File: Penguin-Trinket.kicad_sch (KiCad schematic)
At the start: 17 parts, among them M1 Motor_DC, Q1 NPN, Q2 NPN, Q3 NPN, SW1 SW_Push

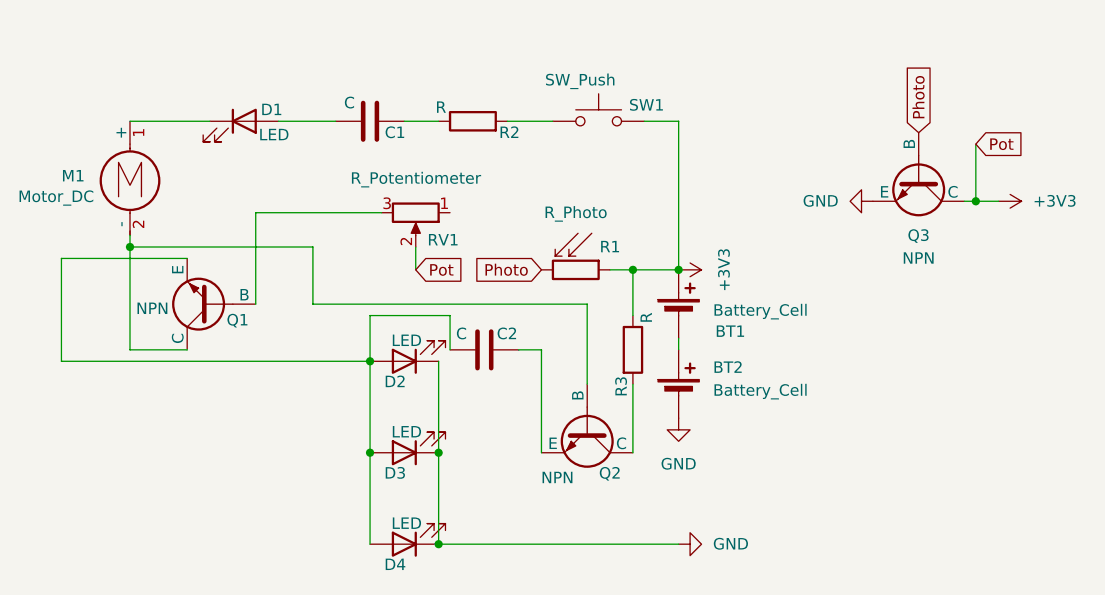
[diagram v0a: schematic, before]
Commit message: redo (trinket v3)
hopefully everything works
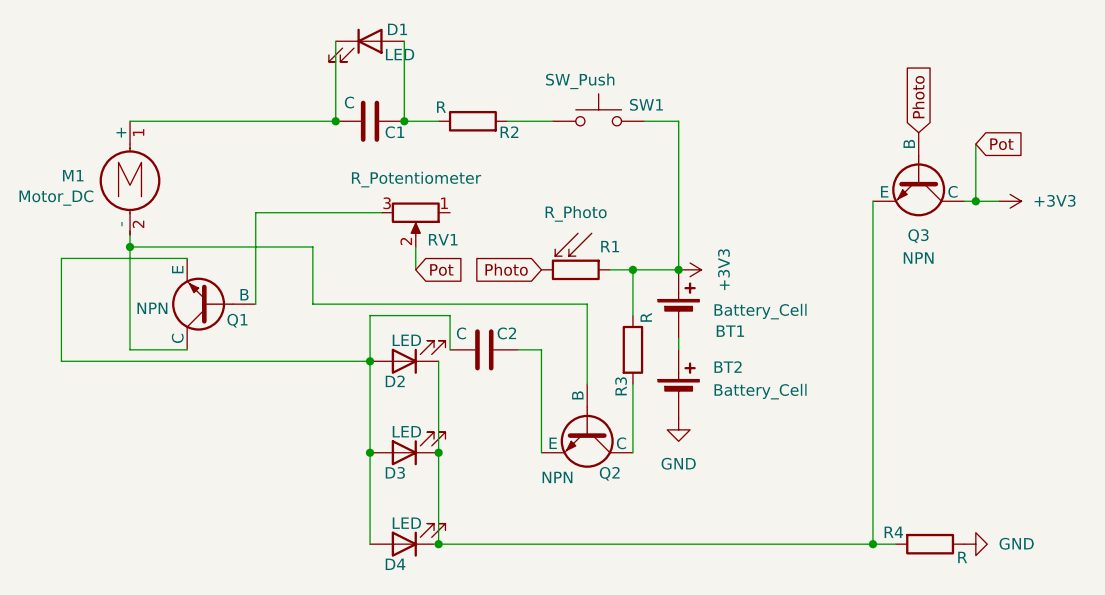
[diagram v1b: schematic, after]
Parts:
- added R4: R, Resistor_THT:R_Axial_DIN0207_L6.3mm_D2.5mm_P7.62mm_Horizontal, symbol Device:R
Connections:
- net GND: now also R4.1; no longer D2.1 (K), D3.1 (K), D4.1 (K), Q3.3 (E)
- net at D1.1 (K), M1.1 (+): now also C1.2
- net at D1.2 (A): now also C1.1, R2.1; no longer C1.2
- new net: D2.1 (K), D3.1 (K), D4.1 (K), Q3.3 (E), R4.2
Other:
- moved on the sheet: D1
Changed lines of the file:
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@@
 	(paper "A4")
+	(junction
+		(at 110.49 63.5)
+		(diameter 0)
+		(color 0 0 0 0)
+	)
 	(junction
 		(at 80.01 77.47)
@@
 	)
 	(junction
-		(at 114.3 110.49)
+		(at 106.68 100.33)
 		(diameter 0)
 		(color 0 0 0 0)
 	)
 	(junction
-		(at 106.68 100.33)
+		(at 114.3 110.49)
 		(diameter 0)
 		(color 0 0 0 0)
@@
 	)
 	(junction
+		(at 102.87 63.5)
+		(diameter 0)
+		(color 0 0 0 0)
+	)
+	(junction
 		(at 106.68 90.17)
 		(diameter 0)
 		(color 0 0 0 0)
 	)
+	(junction
+		(at 162.56 110.49)
+		(diameter 0)
+		(color 0 0 0 0)
+	)
 	(wire
 		(pts
@@
 	(wire
 		(pts
+			(xy 162.56 110.49) (xy 165.1 110.49)
+		)
+		(stroke
+			(width 0)
+			(type default)
+		)
+	)
+	(wire
+		(pts
 			(xy 130.81 83.82) (xy 130.81 92.71)
 		)
@@
 	(wire
 		(pts
-			(xy 96.52 63.5) (xy 102.87 63.5)
-		)
-		(stroke
-			(width 0)
-			(type default)
-		)
-	)
-	(wire
-		(pts
 			(xy 72.39 78.74) (xy 72.39 90.17)
 		)
@@
 	(wire
 		(pts
+			(xy 162.56 110.49) (xy 162.56 72.39)
+		)
+		(stroke
+			(width 0)
+			(type default)
+		)
+	)
+	(wire
+		(pts
 			(xy 107.95 73.66) (xy 93.98 73.66)
 		)
@@
 	(wire
 		(pts
+			(xy 80.01 63.5) (xy 102.87 63.5)
+		)
+		(stroke
+			(width 0)
+			(type default)
+		)
+	)
+	(wire
+		(pts
 			(xy 140.97 87.63) (xy 140.97 88.9)
 		)
@@
 	(wire
 		(pts
-			(xy 140.97 110.49) (xy 114.3 110.49)
+			(xy 114.3 110.49) (xy 162.56 110.49)
 		)
 		(stroke
@@
 	(wire
 		(pts
+			(xy 110.49 63.5) (xy 110.49 54.61)
+		)
+		(stroke
+			(width 0)
+			(type default)
+		)
+	)
+	(wire
+		(pts
 			(xy 80.01 88.9) (xy 86.36 88.9)
 		)
@@
 	(wire
 		(pts
-			(xy 80.01 63.5) (xy 88.9 63.5)
+			(xy 102.87 54.61) (xy 102.87 63.5)
 		)
 		(stroke
@@
 	(symbol
 		(lib_id "Device:LED")
-		(at 92.71 63.5 0)
+		(at 106.68 54.61 0)
 		(unit 1)
 		(exclude_from_sim no)
@@
 		(dnp no)
 		(property "Reference" "D1"
-			(at 95.758 62.23 0)
+			(at 109.728 53.34 0)
 			(effects
 				(font
@@
 		)
 		(property "Value" "LED"
-			(at 96.012 65.024 0)
+			(at 109.982 56.134 0)
 			(effects
 				(font
@@
 		)
 		(property "Footprint" "LED_THT:LED_D5.0mm"
-			(at 92.71 63.5 0)
+			(at 106.68 54.61 0)
 			(effects
 				(font
@@
 		)
 		(property "Datasheet" "~"
-			(at 92.71 63.5 0)
+			(at 106.68 54.61 0)
 			(effects
 				(font
@@
 		)
 		(property "Description" "Light emitting diode"
-			(at 92.71 63.5 0)
+			(at 106.68 54.61 0)
 			(effects
 				(font
@@
 	)
 	(symbol
-		(lib_id "power:GND")
-		(at 162.56 72.39 270)
-		(unit 1)
-		(exclude_from_sim no)
-		(in_bom yes)
-		(on_board yes)
-		(dnp no)
-		(fields_autoplaced yes)
-		(property "Reference" "#PWR04"
-			(at 156.21 72.39 0)
-			(effects
-				(font
-					(size 1.27 1.27)
-				)
-				(hide yes)
-			)
-		)
-		(property "Value" "GND"
-			(at 158.75 72.3899 90)
-			(effects
-				(font
-					(size 1.27 1.27)
-				)
-				(justify right)
-			)
-		)
-		(property "Footprint" ""
-			(at 162.56 72.39 0)
-			(effects
-				(font
-					(size 1.27 1.27)
-				)
-				(hide yes)
-			)
-		)
-		(property "Datasheet" ""
-			(at 162.56 72.39 0)
-			(effects
-				(font
-					(size 1.27 1.27)
-				)
-				(hide yes)
-			)
-		)
-		(property "Description" "Power symbol creates a global label with name \"GND\" , ground"
-			(at 162.56 72.39 0)
-			(effects
-				(font
-					(size 1.27 1.27)
-				)
-				(hide yes)
-			)
-		)
-		(pin "1"
-		)
-		(instances
-			(project ""
-				(path "/8a9e400f-ded9-494b-bf90-341dfd0de4a5"
-					(reference "#PWR04")
-					(unit 1)
-				)
-			)
-		)
-	)
-	(symbol
 		(lib_id "Device:LED")
 		(at 110.49 110.49 180)
@@
 	(symbol
 		(lib_id "power:GND")
-		(at 140.97 110.49 90)
+		(at 172.72 110.49 90)
 		(unit 1)
 		(exclude_from_sim no)
@@
 		(fields_autoplaced yes)
 		(property "Reference" "#PWR05"
-			(at 147.32 110.49 0)
+			(at 179.07 110.49 0)
 			(effects
 				(font
@@
 		)
 		(property "Value" "GND"
-			(at 144.78 110.4899 90)
+			(at 176.53 110.4899 90)
 			(effects
 				(font
@@
 		)
 		(property "Footprint" ""
-			(at 140.97 110.49 0)
+			(at 172.72 110.49 0)
 			(effects
 				(font
@@
 		)
 		(property "Datasheet" ""
-			(at 140.97 110.49 0)
+			(at 172.72 110.49 0)
 			(effects
 				(font
@@
 		)
 		(property "Description" "Power symbol creates a global label with name \"GND\" , ground"
-			(at 140.97 110.49 0)
+			(at 172.72 110.49 0)
 			(effects
 				(font
@@
 					(unit 1)
 				)
+			)
+		)
+	)
+	(symbol
+		(lib_id "Device:R")
+		(at 168.91 110.49 270)
+		(unit 1)
+		(exclude_from_sim no)
+		(in_bom yes)
+		(on_board yes)
+		(dnp no)
+		(property "Reference" "R4"
+			(at 164.846 109.22 90)
+			(effects
+				(font
+					(size 1.27 1.27)
+				)
+			)
+		)
+		(property "Value" "R"
+			(at 172.466 112.014 90)
+			(effects
+				(font
+					(size 1.27 1.27)
+				)
+			)
+		)
+		(property "Footprint" "Resistor_THT:R_Axial_DIN0207_L6.3mm_D2.5mm_P7.62mm_Horizontal"
+			(at 168.91 108.712 90)
+			(effects
+				(font
+					(size 1.27 1.27)
+				)
+				(hide yes)
+			)
+		)
+		(property "Datasheet" "~"
+			(at 168.91 110.49 0)
+			(effects
+				(font
+					(size 1.27 1.27)
+				)
+				(hide yes)
+			)
+		)
+		(property "Description" "Resistor"
+			(at 168.91 110.49 0)
+			(effects
+				(font
+					(size 1.27 1.27)
+				)
+				(hide yes)
+			)
+		)
+		(pin "2"
+		)
+		(pin "1"
+		)
+		(instances
+			(project "Penguin-Trinket"
+				(path "/8a9e400f-ded9-494b-bf90-341dfd0de4a5"
+					(reference "R4")
+					(unit 1)
+				)
